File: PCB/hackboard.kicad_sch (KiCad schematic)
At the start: 208 parts

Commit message: add submodules for pi pico, files for oled
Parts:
- added A1: RaspberryPi_Pico, Module:RaspberryPi_Pico_Common_Unspecified, symbol MCU_Module:RaspberryPi_Pico
- added J1: Conn_01x04, Connector_PinSocket_2.54mm:PinSocket_1x04_P2.54mm_Vertical, symbol Connector_Generic:Conn_01x04
- added U1: MCP23008-xP, Package_DIP:DIP-18_W7.62mm, symbol Interface_Expansion:MCP23008-xP
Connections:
- net col22 is gone; now on net col21: K_36.1 (COL), K_57.1 (COL), K_90.1 (COL)
- net col0: now also A1.7 (GPIO5)
- net col1: now also A1.9 (GPIO6)
- net col10: now also A1.20 (GPIO15)
- net col11: now also A1.26 (GPIO20)
- net col12: now also A1.27 (GPIO21)
- net col13: now also A1.29 (GPIO22)
- net col14: now also A1.31 (GPIO26_ADC0)
- net col15: now also A1.32 (GPIO27_ADC1)
- net col16: now also A1.34 (GPIO28_ADC2)
- net col17: now also U1.10 (GP0)
- net col19: now also K_34.1 (COL), K_55.1 (COL), K_72.1 (COL), K_88.1 (COL), U1.12 (GP2); no longer K_102.1 (COL), K_33.1 (COL), K_54.1 (COL), K_71.1 (COL), K_87.1 (COL)
- net col2: now also A1.10 (GPIO7)
- net col20: now also K_103.1 (COL), K_35.1 (COL), K_56.1 (COL), K_73.1 (COL), K_89.1 (COL), U1.13 (GP3); no longer K_34.1 (COL), K_55.1 (COL), K_72.1 (COL), K_88.1 (COL)
- net col21: now also U1.14 (GP4); no longer K_103.1 (COL), K_35.1 (COL), K_56.1 (COL), K_73.1 (COL), K_89.1 (COL)
- net col3: now also A1.11 (GPIO8)
- net col4: now also A1.12 (GPIO9)
- net col5: now also A1.14 (GPIO10)
- net col6: now also A1.15 (GPIO11)
- net col7: now also A1.16 (GPIO12)
- net col8: now also A1.17 (GPIO13)
- net col9: now also A1.19 (GPIO14)
- net row0: now also A1.1 (GPIO0)
- net row1: now also A1.2 (GPIO1)
- net row2: now also A1.4 (GPIO2)
- net row3: now also A1.5 (GPIO3)
- net row4: now also A1.6 (GPIO4)
- new net: A1.13 (GND), A1.18 (GND), A1.23 (GND), A1.28 (GND), A1.3 (GND), A1.38 (GND), A1.8 (GND)
- new net: U1.3 (A2), U1.5 (A0)
- new net +5V: A1.40 (VBUS), J1.3 (Pin_3), U1.18 (VDD), U1.6 (~{RESET})
- new net GND: J1.4 (Pin_4), U1.4 (A1), U1.9 (VSS)
- new net col18: K_102.1 (COL), K_33.1 (COL), K_54.1 (COL), K_71.1 (COL), K_87.1 (COL), U1.11 (GP1)
- new net i2c0_scl: A1.22 (GPIO17), U1.1 (SCL)
- new net i2c0_sda: A1.21 (GPIO16), U1.2 (SDA)
- new net i2c1_scl: A1.25 (GPIO19), J1.2 (Pin_2)
- new net i2c1_sda: A1.24 (GPIO18), J1.1 (Pin_1)
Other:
- note added: "IO Expander"
- note added: "Keyboard"
- note added: "OLED Display"
- note added: "RP2040 MCU"
- moved on the sheet: D_0, D_1, D_10, D_100, D_101, D_102, D_103, D_11, D_12, D_13, D_14, D_15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

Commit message: add 3d models for all key switches and components
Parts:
- A1: footprint Module:RaspberryPi_Pico_Common_Unspecified -> Library_Edited:RaspberryPi_Pico_Common_Unspecified
- J1: footprint Connector_PinSocket_2.54mm:PinSocket_1x04_P2.54mm_Vertical -> Library_Edited:PinSocket_1x04_P2.54mm_Vertical_OLED
- K_0, K_1, K_10, K_100, K_101, K_103, K_11, K_12, K_13, K_14, K_15, K_16, K_17, K_18, K_19, K_2, K_20, K_21, K_22, K_23, K_24, K_25, K_26, K_27, K_28, K_3, K_30, K_31, K_32, K_33, K_34, K_35, K_36, K_38, K_39, K_4, K_40, K_41, K_42, K_43, K_44, K_45, K_46, K_47, K_48, K_49, K_5, K_51, K_52, K_53, K_54, K_55, K_56, K_59, K_6, K_60, K_61, K_62, K_63, K_64, K_65, K_66, K_67, K_68, K_69, K_7, K_71, K_72, K_73, K_75, K_76, K_77, K_78, K_79, K_8, K_80, K_81, K_82, K_83, K_84, K_86, K_87, K_88, K_89, K_9, K_99: footprint Button_Switch_Keyboard:SW_Cherry_MX_1.00u_PCB -> Library_Edited:SW_Cherry_MX_1.00u_PCB
- K_102, K_29, K_57, K_90: footprint Button_Switch_Keyboard:SW_Cherry_MX_2.00u_PCB -> Library_Edited:SW_Cherry_MX_2.00u_PCB
- K_37, K_50: footprint Button_Switch_Keyboard:SW_Cherry_MX_1.50u_PCB -> Library_Edited:SW_Cherry_MX_1.50u_PCB
- K_58: footprint Button_Switch_Keyboard:SW_Cherry_MX_1.75u_PCB -> Library_Edited:SW_Cherry_MX_1.75u_PCB
- K_70, K_74: footprint Button_Switch_Keyboard:SW_Cherry_MX_2.25u_PCB -> Library_Edited:SW_Cherry_MX_2.25u_PCB
- K_85: footprint Button_Switch_Keyboard:SW_Cherry_MX_2.75u_PCB -> Library_Edited:SW_Cherry_MX_2.75u_PCB
- K_91, K_92, K_93, K_95, K_96, K_97, K_98: footprint Button_Switch_Keyboard:SW_Cherry_MX_1.25u_PCB -> Library_Edited:SW_Cherry_MX_1.25u_PCB
- K_94: footprint Button_Switch_Keyboard:SW_Cherry_MX_6.25u_PCB -> Library_Edited:SW_Cherry_MX_6.25u_PCB

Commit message: silkscreen art and mounting holes
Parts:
- K_57, K_90: footprint Library_Edited:SW_Cherry_MX_2.00u_PCB -> Library_Edited:SW_Cherry_MX_2.00u_PCB_r1
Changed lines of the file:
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@@
 			)
 		)
-		(property "Footprint" "Library_Edited:SW_Cherry_MX_2.00u_PCB"
+		(property "Footprint" "Library_Edited:SW_Cherry_MX_2.00u_PCB_r1"
 			(at 563.88 88.9 0)
 			(effects
@@
 			)
 		)
-		(property "Footprint" "Library_Edited:SW_Cherry_MX_2.00u_PCB"
+		(property "Footprint" "Library_Edited:SW_Cherry_MX_2.00u_PCB_r1"
 			(at 563.88 139.7 0)
 			(effects

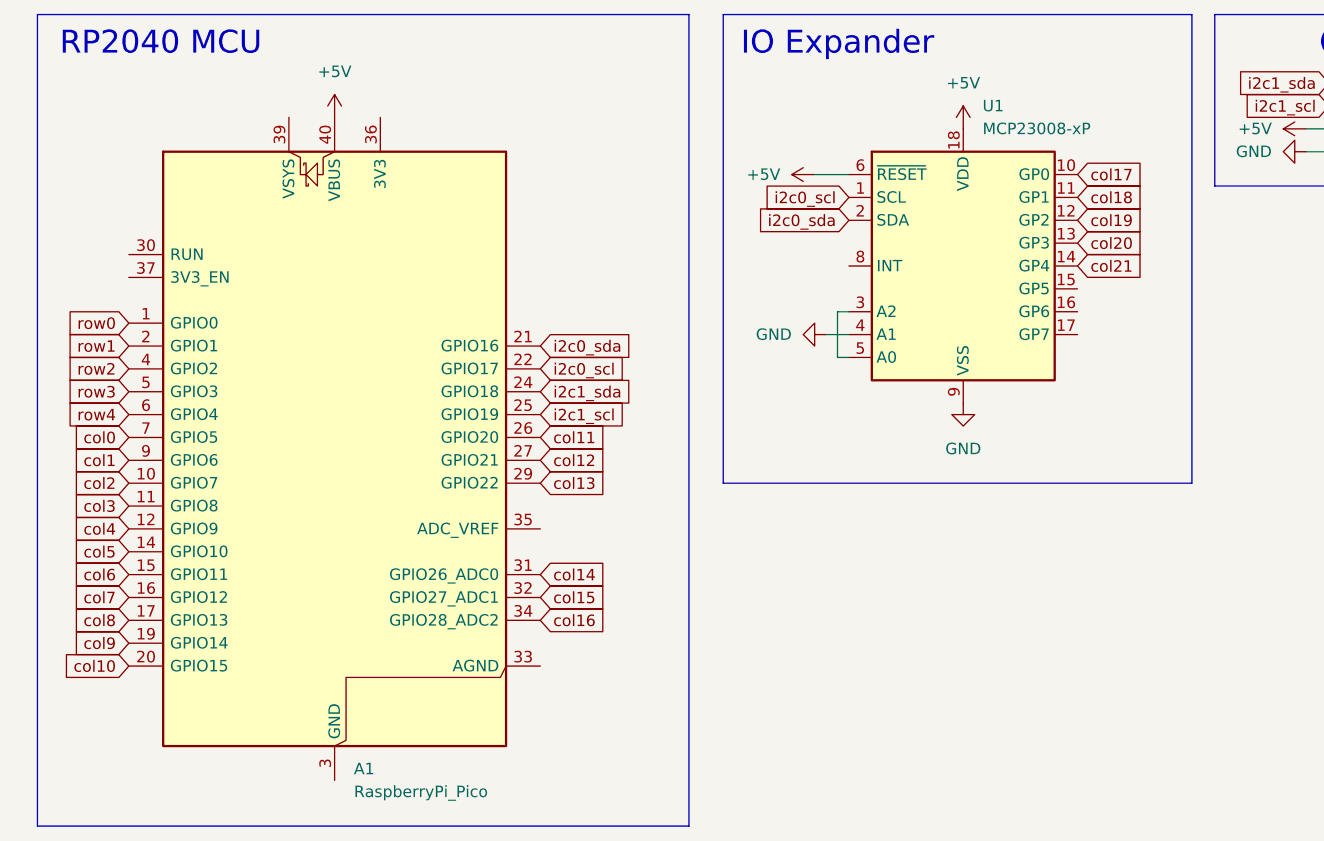
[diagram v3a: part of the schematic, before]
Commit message: fix missing row5 connection on pcb
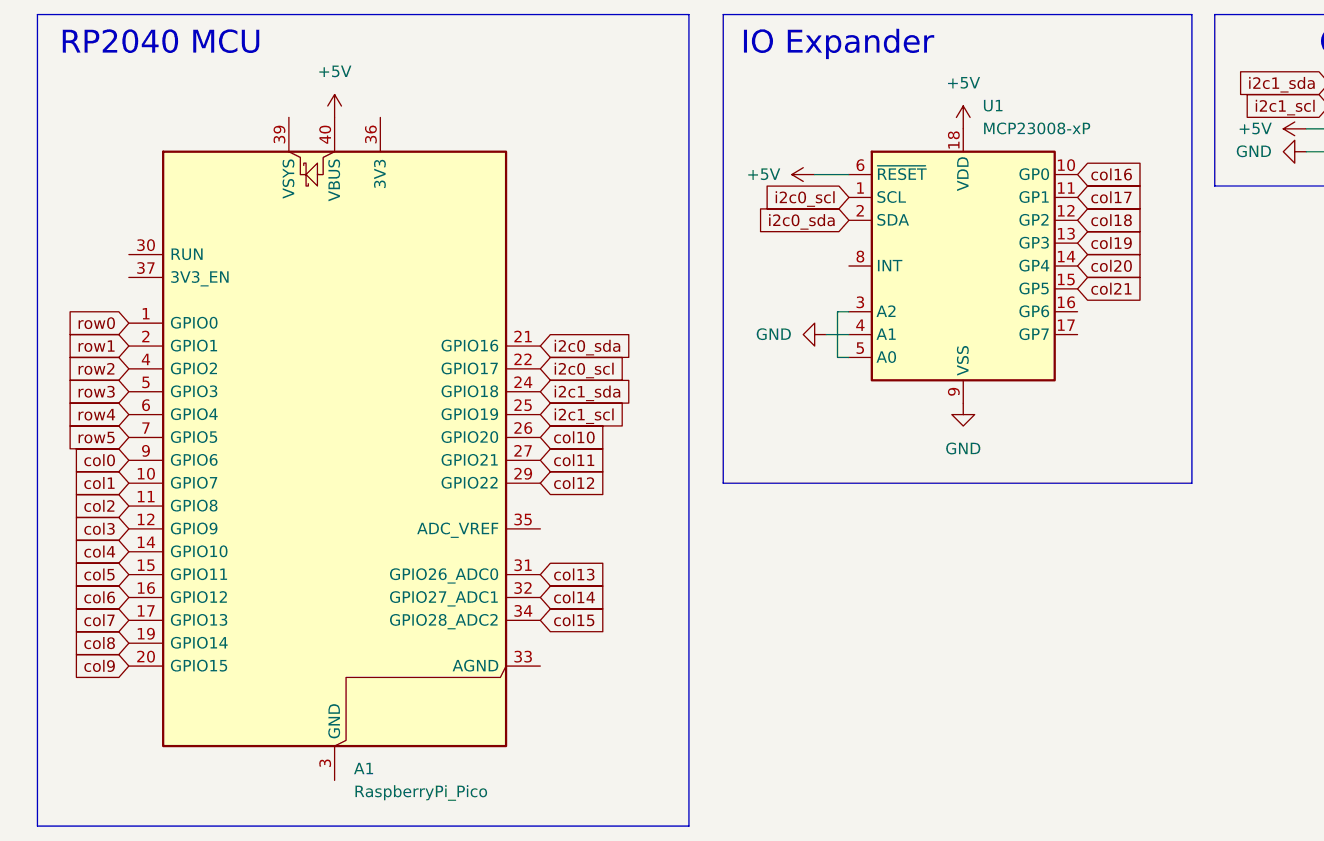
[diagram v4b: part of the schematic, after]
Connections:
- net col0: now also A1.9 (GPIO6); no longer A1.7 (GPIO5)
- net col1: now also A1.10 (GPIO7); no longer A1.9 (GPIO6)
- net col10: now also A1.26 (GPIO20); no longer A1.20 (GPIO15)
- net col11: now also A1.27 (GPIO21); no longer A1.26 (GPIO20)
- net col12: now also A1.29 (GPIO22); no longer A1.27 (GPIO21)
- net col13: now also A1.31 (GPIO26_ADC0); no longer A1.29 (GPIO22)
- net col14: now also A1.32 (GPIO27_ADC1); no longer A1.31 (GPIO26_ADC0)
- net col15: now also A1.34 (GPIO28_ADC2); no longer A1.32 (GPIO27_ADC1)
- net col16: now also U1.10 (GP0); no longer A1.34 (GPIO28_ADC2)
- net col17: now also U1.11 (GP1); no longer U1.10 (GP0)
- net col18: now also U1.12 (GP2); no longer U1.11 (GP1)
- net col19: now also U1.13 (GP3); no longer U1.12 (GP2)
- net col2: now also A1.11 (GPIO8); no longer A1.10 (GPIO7)
- net col20: now also U1.14 (GP4); no longer U1.13 (GP3)
- net col21: now also U1.15 (GP5); no longer U1.14 (GP4)
- net col3: now also A1.12 (GPIO9); no longer A1.11 (GPIO8)
- net col4: now also A1.14 (GPIO10); no longer A1.12 (GPIO9)
- net col5: now also A1.15 (GPIO11); no longer A1.14 (GPIO10)
- net col6: now also A1.16 (GPIO12); no longer A1.15 (GPIO11)
- net col7: now also A1.17 (GPIO13); no longer A1.16 (GPIO12)
- net col8: now also A1.19 (GPIO14); no longer A1.17 (GPIO13)
- net col9: now also A1.20 (GPIO15); no longer A1.19 (GPIO14)
- net row5: now also A1.7 (GPIO5)
